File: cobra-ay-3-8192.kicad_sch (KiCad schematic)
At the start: 28 parts, among them J1 C96ABC, J2 Conn_01x10, J4 Conn_Coaxial, J5 Conn_Coaxial, Q1 BC239, U1 AY-3-8192, U2 74LS138, U3 74LS02, U4 74LS00, U5 74LS74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

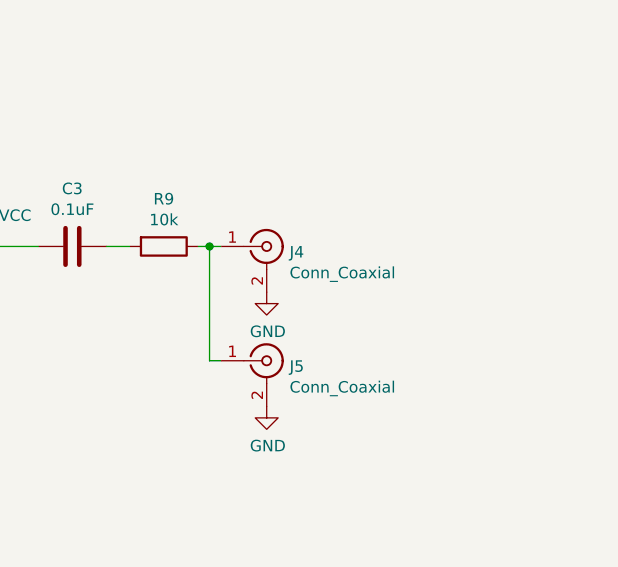
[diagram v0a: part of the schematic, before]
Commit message: Fix issues with audio input/output
Swap RCA connector pins, move RCA connectors closer to board edge, and
add resistors R10 and R11 to input audio.
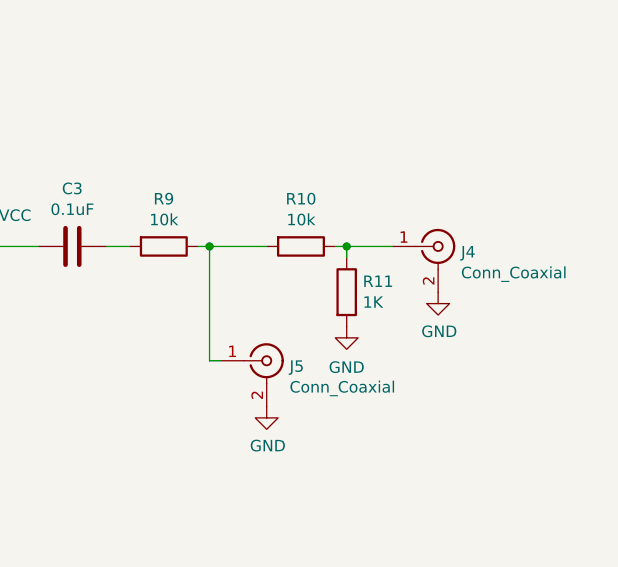
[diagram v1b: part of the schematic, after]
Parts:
- added R10: 10k, Resistor_THT:R_Axial_DIN0204_L3.6mm_D1.6mm_P7.62mm_Horizontal, symbol Device:R
- added R11: 1K, Resistor_THT:R_Axial_DIN0204_L3.6mm_D1.6mm_P7.62mm_Horizontal, symbol Device:R
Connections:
- net GND: now also R11.2
- net at J5.1 (In), R9.1: now also R10.2; no longer J4.1 (In)
- new net: J4.1 (In), R10.1, R11.1
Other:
- moved on the sheet: J4
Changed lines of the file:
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@@
   (junction (at 171.45 148.59) (diameter 0) (color 0 0 0 0)
   )
+  (junction (at 182.88 148.59) (diameter 0) (color 0 0 0 0)
+  )
+  (junction (at 91.44 109.22) (diameter 0) (color 0 0 0 0)
+  )
+  (junction (at 26.67 171.45) (diameter 0) (color 0 0 0 0)
+  )
+  (junction (at 52.07 34.29) (diameter 0) (color 0 0 0 0)
+  )
+  (junction (at 193.04 76.2) (diameter 0) (color 0 0 0 0)
+  )
+  (junction (at 133.35 78.74) (diameter 0) (color 0 0 0 0)
+  )
+  (junction (at 205.74 76.2) (diameter 0) (color 0 0 0 0)
+  )
+  (junction (at 194.31 156.21) (diameter 0) (color 0 0 0 0)
+  )
+  (junction (at 133.35 71.12) (diameter 0) (color 0 0 0 0)
+  )
+  (junction (at 46.99 173.99) (diameter 0) (color 0 0 0 0)
+  )
+  (junction (at 194.31 148.59) (diameter 0) (color 0 0 0 0)
+  )
+  (junction (at 205.74 156.21) (diameter 0) (color 0 0 0 0)
+  )
+  (junction (at 59.69 171.45) (diameter 0) (color 0 0 0 0)
+  )
+  (junction (at 36.83 34.29) (diameter 0) (color 0 0 0 0)
+  )
+  (junction (at 25.4 138.43) (diameter 0) (color 0 0 0 0)
+  )
+  (junction (at 193.04 86.36) (diameter 0) (color 0 0 0 0)
+  )
+  (junction (at 34.29 34.29) (diameter 0) (color 0 0 0 0)
+  )
+  (junction (at 49.53 34.29) (diameter 0) (color 0 0 0 0)
+  )
+  (junction (at 193.04 81.28) (diameter 0) (color 0 0 0 0)
+  )
+  (junction (at 255.27 34.29) (diameter 0) (color 0 0 0 0)
+  )
+  (junction (at 257.81 34.29) (diameter 0) (color 0 0 0 0)
+  )
+  (junction (at 71.12 135.89) (diameter 0) (color 0 0 0 0)
+  )
+  (junction (at 182.88 156.21) (diameter 0) (color 0 0 0 0)
+  )
+  (junction (at 59.69 173.99) (diameter 0) (color 0 0 0 0)
+  )
   (junction (at 242.57 80.01) (diameter 0) (color 0 0 0 0)
   )
-  (junction (at 182.88 148.59) (diameter 0) (color 0 0 0 0)
-  )
-  (junction (at 91.44 109.22) (diameter 0) (color 0 0 0 0)
-  )
-  (junction (at 26.67 171.45) (diameter 0) (color 0 0 0 0)
-  )
-  (junction (at 52.07 34.29) (diameter 0) (color 0 0 0 0)
-  )
-  (junction (at 193.04 76.2) (diameter 0) (color 0 0 0 0)
-  )
-  (junction (at 133.35 78.74) (diameter 0) (color 0 0 0 0)
-  )
-  (junction (at 205.74 76.2) (diameter 0) (color 0 0 0 0)
-  )
-  (junction (at 194.31 156.21) (diameter 0) (color 0 0 0 0)
-  )
-  (junction (at 133.35 71.12) (diameter 0) (color 0 0 0 0)
-  )
-  (junction (at 46.99 173.99) (diameter 0) (color 0 0 0 0)
-  )
-  (junction (at 194.31 148.59) (diameter 0) (color 0 0 0 0)
-  )
-  (junction (at 205.74 156.21) (diameter 0) (color 0 0 0 0)
-  )
-  (junction (at 59.69 171.45) (diameter 0) (color 0 0 0 0)
-  )
-  (junction (at 36.83 34.29) (diameter 0) (color 0 0 0 0)
-  )
-  (junction (at 25.4 138.43) (diameter 0) (color 0 0 0 0)
-  )
-  (junction (at 193.04 86.36) (diameter 0) (color 0 0 0 0)
-  )
-  (junction (at 34.29 34.29) (diameter 0) (color 0 0 0 0)
-  )
-  (junction (at 49.53 34.29) (diameter 0) (color 0 0 0 0)
-  )
-  (junction (at 193.04 81.28) (diameter 0) (color 0 0 0 0)
-  )
-  (junction (at 255.27 34.29) (diameter 0) (color 0 0 0 0)
-  )
-  (junction (at 257.81 34.29) (diameter 0) (color 0 0 0 0)
-  )
-  (junction (at 71.12 135.89) (diameter 0) (color 0 0 0 0)
-  )
-  (junction (at 182.88 156.21) (diameter 0) (color 0 0 0 0)
-  )
-  (junction (at 59.69 173.99) (diameter 0) (color 0 0 0 0)
-  )
   (junction (at 80.01 162.56) (diameter 0) (color 0 0 0 0)
+  )
+  (junction (at 257.81 80.01) (diameter 0) (color 0 0 0 0)
   )
   (no_connect (at 191.77 33.02))
@@
     (stroke (width 0) (type default) (color 0 0 0 0))
   )
+  (wire (pts (xy 257.81 80.01) (xy 262.89 80.01))
+    (stroke (width 0) (type default) (color 0 0 0 0))
+  )
   (wire (pts (xy 34.29 34.29) (xy 36.83 34.29))
     (stroke (width 0) (type default) (color 0 0 0 0))
@@
     (stroke (width 0) (type default) (color 0 0 0 0))
   )
-  (wire (pts (xy 242.57 80.01) (xy 243.84 80.01))
-    (stroke (width 0) (type default) (color 0 0 0 0))
-  )
   (wire (pts (xy 111.76 97.79) (xy 111.76 116.84))
     (stroke (width 0) (type default) (color 0 0 0 0))
@@
     (stroke (width 0) (type default) (color 0 0 0 0))
   )
+  (wire (pts (xy 257.81 80.01) (xy 257.81 81.28))
+    (stroke (width 0) (type default) (color 0 0 0 0))
+  )
   (wire (pts (xy 194.31 148.59) (xy 182.88 148.59))
     (stroke (width 0) (type default) (color 0 0 0 0))
@@
     (stroke (width 0) (type default) (color 0 0 0 0))
   )
+  (wire (pts (xy 256.54 80.01) (xy 257.81 80.01))
+    (stroke (width 0) (type default) (color 0 0 0 0))
+  )
   (wire (pts (xy 59.69 173.99) (xy 59.69 171.45))
     (stroke (width 0) (type default) (color 0 0 0 0))
@@
   )
   (wire (pts (xy 109.22 111.76) (xy 142.24 111.76))
+    (stroke (width 0) (type default) (color 0 0 0 0))
+  )
+  (wire (pts (xy 242.57 80.01) (xy 248.92 80.01))
     (stroke (width 0) (type default) (color 0 0 0 0))
   )
@@
     (pin "1")
   )
-  (symbol (lib_id "Connector:Conn_Coaxial") (at 248.92 80.01 0) (unit 1)
-    (in_bom yes) (on_board yes)
-    (property "Reference" "J4" (id 0) (at 251.46 80.645 0)
-      (effects (font (size 1.27 1.27)) (justify left))
-    )
-    (property "Value" "Conn_Coaxial" (id 1) (at 251.46 82.9564 0)
-      (effects (font (size 1.27 1.27)) (justify left))
-    )
-    (property "Footprint" "RCJ-04:RCJ-04" (id 2) (at 248.92 80.01 0)
-      (effects (font (size 1.27 1.27)) hide)
-    )
-    (property "Datasheet" " ~" (id 3) (at 248.92 80.01 0)
+  (symbol (lib_id "Connector:Conn_Coaxial") (at 267.97 80.01 0) (unit 1)
+    (in_bom yes) (on_board yes)
+    (property "Reference" "J4" (id 0) (at 270.51 80.645 0)
+      (effects (font (size 1.27 1.27)) (justify left))
+    )
+    (property "Value" "Conn_Coaxial" (id 1) (at 270.51 82.9564 0)
+      (effects (font (size 1.27 1.27)) (justify left))
+    )
+    (property "Footprint" "RCJ-04:RCJ-04" (id 2) (at 267.97 80.01 0)
+      (effects (font (size 1.27 1.27)) hide)
+    )
+    (property "Datasheet" " ~" (id 3) (at 267.97 80.01 0)
       (effects (font (size 1.27 1.27)) hide)
     )
@@
     (pin "2")
   )
-  (symbol (lib_id "power:GND") (at 248.92 85.09 0) (unit 1)
-    (in_bom yes) (on_board yes)
-    (property "Reference" "#PWR010" (id 0) (at 248.92 91.44 0)
-      (effects (font (size 1.27 1.27)) hide)
-    )
-    (property "Value" "GND" (id 1) (at 249.047 89.4842 0))
-    (property "Footprint" "" (id 2) (at 248.92 85.09 0)
-      (effects (font (size 1.27 1.27)) hide)
-    )
-    (property "Datasheet" "" (id 3) (at 248.92 85.09 0)
+  (symbol (lib_id "power:GND") (at 267.97 85.09 0) (unit 1)
+    (in_bom yes) (on_board yes)
+    (property "Reference" "#PWR010" (id 0) (at 267.97 91.44 0)
+      (effects (font (size 1.27 1.27)) hide)
+    )
+    (property "Value" "GND" (id 1) (at 268.097 89.4842 0))
+    (property "Footprint" "" (id 2) (at 267.97 85.09 0)
+      (effects (font (size 1.27 1.27)) hide)
+    )
+    (property "Datasheet" "" (id 3) (at 267.97 85.09 0)
       (effects (font (size 1.27 1.27)) hide)
     )
@@
     (pin "1")
   )
+  (symbol (lib_id "Device:R") (at 252.73 80.01 270) (unit 1)
+    (in_bom yes) (on_board yes)
+    (property "Reference" "R10" (id 0) (at 252.73 74.7522 90))
+    (property "Value" "10k" (id 1) (at 252.73 77.0636 90))
+    (property "Footprint" "Resistor_THT:R_Axial_DIN0204_L3.6mm_D1.6mm_P7.62mm_Horizontal" (id 2) (at 252.73 78.232 90)
+      (effects (font (size 1.27 1.27)) hide)
+    )
+    (property "Datasheet" "~" (id 3) (at 252.73 80.01 0)
+      (effects (font (size 1.27 1.27)) hide)
+    )
+    (pin "1")
+    (pin "2")
+  )
+  (symbol (lib_id "power:GND") (at 257.81 88.9 0) (unit 1)
+    (in_bom yes) (on_board yes) (fields_autoplaced)
+    (property "Reference" "#PWR0101" (id 0) (at 257.81 95.25 0)
+      (effects (font (size 1.27 1.27)) hide)
+    )
+    (property "Value" "GND" (id 1) (at 257.81 93.4625 0))
+    (property "Footprint" "" (id 2) (at 257.81 88.9 0)
+      (effects (font (size 1.27 1.27)) hide)
+    )
+    (property "Datasheet" "" (id 3) (at 257.81 88.9 0)
+      (effects (font (size 1.27 1.27)) hide)
+    )
+    (pin "1")
+  )
+  (symbol (lib_id "Device:R") (at 257.81 85.09 0) (unit 1)
+    (in_bom yes) (on_board yes)
+    (property "Reference" "R11" (id 0) (at 259.588 83.9216 0)
+      (effects (font (size 1.27 1.27)) (justify left))
+    )
+    (property "Value" "1K" (id 1) (at 259.588 86.233 0)
+      (effects (font (size 1.27 1.27)) (justify left))
+    )
+    (property "Footprint" "Resistor_THT:R_Axial_DIN0204_L3.6mm_D1.6mm_P7.62mm_Horizontal" (id 2) (at 256.032 85.09 90)
+      (effects (font (size 1.27 1.27)) hide)
+    )
+    (property "Datasheet" "~" (id 3) (at 257.81 85.09 0)
+      (effects (font (size 1.27 1.27)) hide)
+    )
+    (pin "1")
+    (pin "2")
+  )
   (sheet_instances
     (path "/" (page "1"))
@@
       (reference "#PWR033") (unit 1) (value "GND") (footprint "")
     )
+    (path "/69947ffd-f299-4ae4-805a-533972393e84"
+      (reference "#PWR0101") (unit 1) (value "GND") (footprint "")
+    )
     (path "/00000000-0000-0000-0000-00006163e075"
       (reference "C1") (unit 1) (value "0.1uF") (footprint "Capacitor_THT:C_Disc_D5.0mm_W2.5mm_P5.00mm")
@@
       (reference "R9") (unit 1) (value "10k") (footprint "Resistor_THT:R_Axial_DIN0204_L3.6mm_D1.6mm_P7.62mm_Horizontal")
     )
+    (path "/5f30f18a-2eb5-4274-9d3d-af9601238118"
+      (reference "R10") (unit 1) (value "10k") (footprint "Resistor_THT:R_Axial_DIN0204_L3.6mm_D1.6mm_P7.62mm_Horizontal")
+    )
+    (path "/fcc5dc88-6468-4924-8717-a5590e40fd9e"
+      (reference "R11") (unit 1) (value "1K") (footprint "Resistor_THT:R_Axial_DIN0204_L3.6mm_D1.6mm_P7.62mm_Horizontal")
+    )
     (path "/00000000-0000-0000-0000-0000615e45e3"
